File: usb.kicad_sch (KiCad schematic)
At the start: 7 parts, among them J2 TYPE-C 16PIN 2MD(073), U4 USBLC6-2P6, U5 USBLC6-2P6

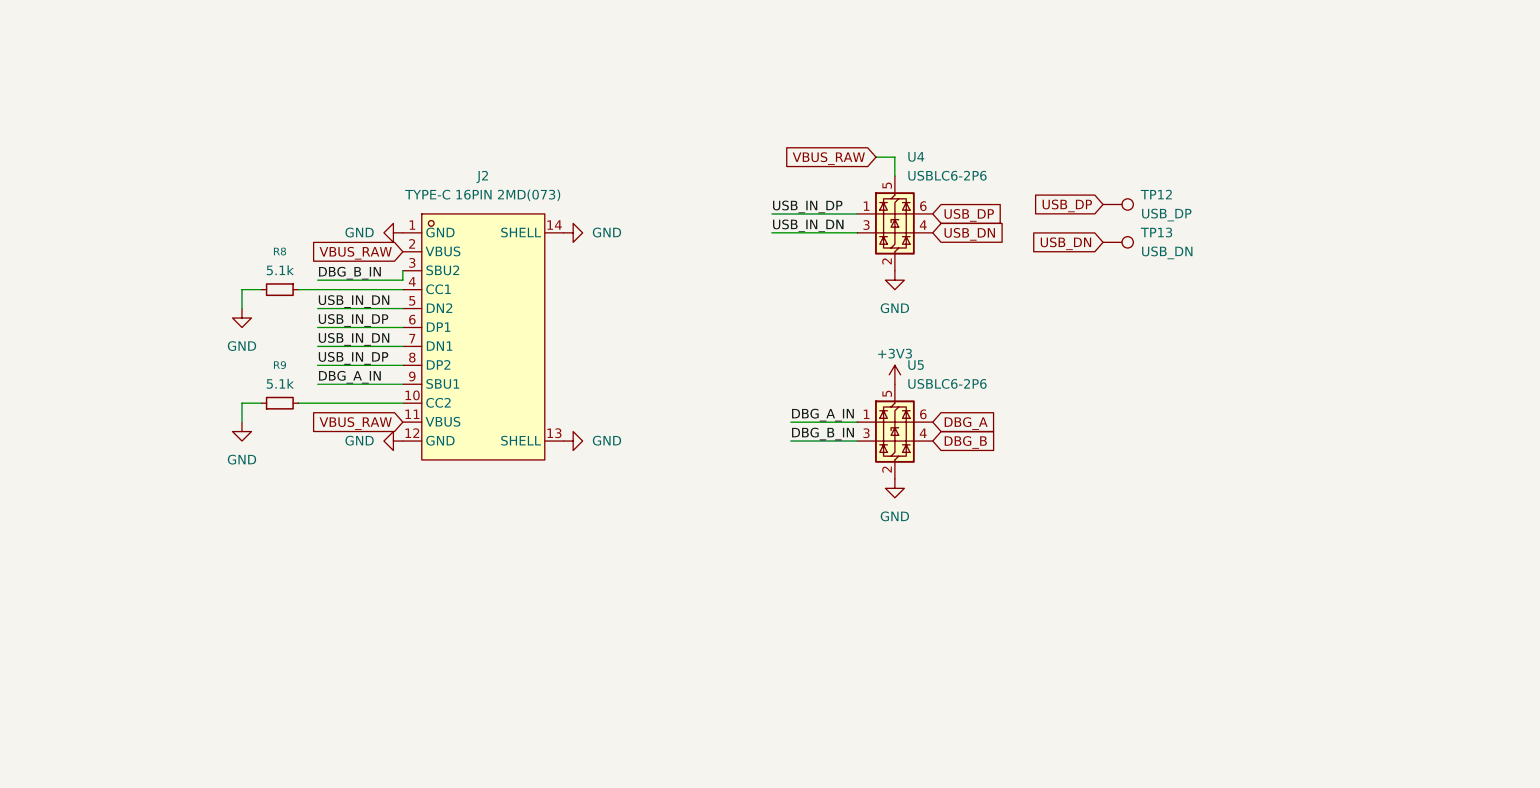
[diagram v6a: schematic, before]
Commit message: prepare schematic for devboard
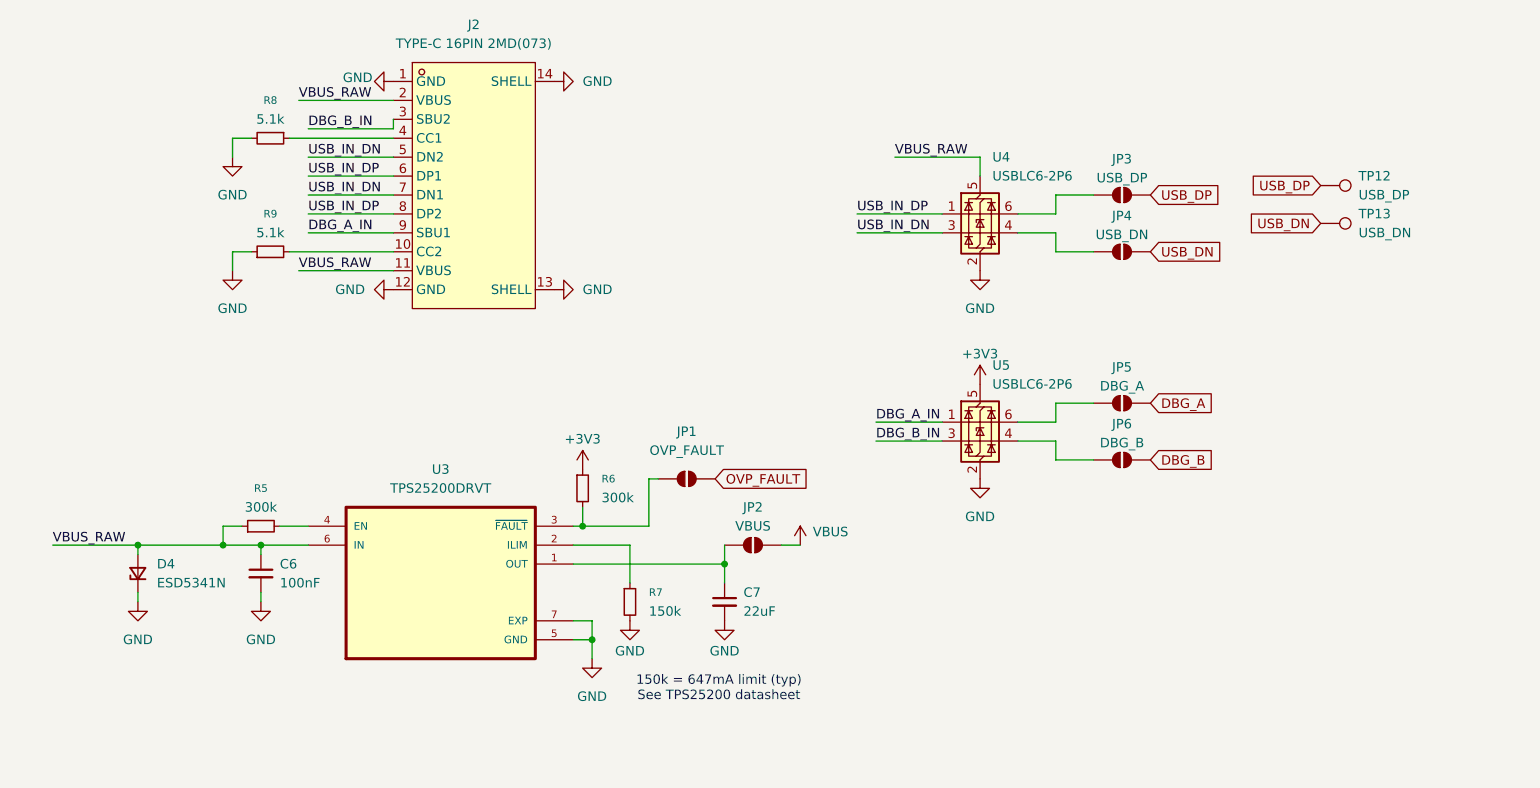
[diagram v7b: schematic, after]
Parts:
- added C6: 100nF, Capacitor_SMD:C_0402_1005Metric, symbol Device:C_Small
- added C7: 22uF, Capacitor_SMD:C_0603_1608Metric, symbol Device:C_Small
- added D4: ESD5341N, Diode_SMD:D_SOD-882, symbol Device:D_Zener_Small
- added JP1: OVP_FAULT, Jumper:SolderJumper-2_P1.3mm_Open_Pad1.0x1.5mm, symbol Jumper:SolderJumper_2_Open
- added JP2: VBUS, Jumper:SolderJumper-2_P1.3mm_Open_Pad1.0x1.5mm, symbol Jumper:SolderJumper_2_Open
- added JP3: USB_DP, Jumper:SolderJumper-2_P1.3mm_Open_Pad1.0x1.5mm, symbol Jumper:SolderJumper_2_Open
- added JP4: USB_DN, Jumper:SolderJumper-2_P1.3mm_Open_Pad1.0x1.5mm, symbol Jumper:SolderJumper_2_Open
- added JP5: DBG_A, Jumper:SolderJumper-2_P1.3mm_Open_Pad1.0x1.5mm, symbol Jumper:SolderJumper_2_Open
- added JP6: DBG_B, Jumper:SolderJumper-2_P1.3mm_Open_Pad1.0x1.5mm, symbol Jumper:SolderJumper_2_Open
- added R5, R6: 300k, Resistor_SMD:R_0603_1608Metric, symbol Device:R_Small
- added R7: 150k, Resistor_SMD:R_0603_1608Metric, symbol Device:R_Small
- added U3: TPS25200DRVT, TPS25200DRVT:SON65P200X200X80-7N, symbol TPS25200DRVT:TPS25200DRVT
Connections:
- net +3V3: now also R6.1
- net DBG_A: now also JP5.2 (B); no longer U5.6 (I/O1)
- net DBG_B: now also JP6.2 (B); no longer U5.4 (I/O2)
- net GND: now also C6.2, C7.2, D4.1 (K), R7.2, U3.5 (GND), U3.7 (EXP)
- net USB_DN: now also JP4.2 (B); no longer U4.4 (I/O2)
- net USB_DP: now also JP3.2 (B); no longer U4.6 (I/O1)
- net VBUS_RAW: now also C6.1, D4.2 (A), R5.1, U3.6 (IN)
- new net: C7.1, JP2.1 (A), U3.1 (OUT)
- new net: JP4.1 (A), U4.4 (I/O2)
- new net: JP1.1 (A), R6.2, U3.3 (~{FAULT})
- new net: R7.1, U3.2 (ILIM)
- new net: R5.2, U3.4 (EN)
- new net: JP3.1 (A), U4.6 (I/O1)
- new net: JP6.1 (A), U5.4 (I/O2)
- new net: JP5.1 (A), U5.6 (I/O1)
- new net OVP_FAULT: JP1.2 (B)
- new net VBUS: JP2.2 (B)
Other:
- note added: "150k = 647mA limit (typ) See TPS25200 datasheet"
- moved on the sheet: J2, R8, R9, TP12, TP13, U4, U5

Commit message: huge progress on bentoboard, schematic fixes
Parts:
- added JP44: USB_3V3, Jumper:SolderJumper-2_P1.3mm_Open_Pad1.0x1.5mm, symbol Jumper:SolderJumper_2_Open
- JP1: value OVP_FAULT -> USB_OVP_FAULT
- JP2: value VBUS -> USB_VBUS
- JP5: value DBG_A -> USB_DBG_A
- JP6: value DBG_B -> USB_DBG_B
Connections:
- net +3V3: now also JP44.1 (A); no longer R6.1, U5.5 (VBUS)
- net USB_IN_DN: now also U4.1 (I/O1); no longer U4.3 (I/O2)
- net USB_IN_DP: now also U4.3 (I/O2); no longer U4.1 (I/O1)
- net USB_PROT_DN: now reaches JP4.1 (A)
- net USB_PROT_DN: now also U4.6 (I/O1); no longer U4.4 (I/O2)
- net USB_PROT_DP: now reaches JP3.1 (A)
- net USB_PROT_DP: now also U4.4 (I/O2); no longer U4.6 (I/O1)
- new net USB_3V3_IN: JP44.2 (B), R6.1, U5.5 (VBUS)
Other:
- moved on the sheet: C6, C7, D4, JP1, JP2, JP3, JP4, JP5, JP6, R5, R6, R7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
